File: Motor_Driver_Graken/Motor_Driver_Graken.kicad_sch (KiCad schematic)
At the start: 0 parts

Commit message: Break resistor and IC details
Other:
- added sheet IC Details (IC_Details.kicad_sch)
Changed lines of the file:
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@@
+	)
+	(sheet
+		(at 236.982 80.01)
+		(size 43.434 33.274)
+		(exclude_from_sim no)
+		(in_bom yes)
+		(on_board yes)
+		(dnp no)
+		(fields_autoplaced yes)
+		(stroke
+			(width 0.1524)
+			(type solid)
+		)
+		(fill
+			(color 0 0 0 0.0000)
+		)
+		(property "Sheetname" "IC Details"
+			(at 236.982 79.2984 0)
+			(effects
+				(font
+					(size 1.27 1.27)
+				)
+				(justify left bottom)
+			)
+		)
+		(property "Sheetfile" "IC_Details.kicad_sch"
+			(at 236.982 113.8686 0)
+			(effects
+				(font
+					(size 1.27 1.27)
+				)
+				(justify left top)
+			)
+		)
+		(instances
+			(project "Motor_Driver_Graken"
+				(path "/7c9d4969-3cbd-46ca-8216-6f71fd9792b9"
+					(page "9")
+				)
+			)
+		)
 	)
 	(sheet

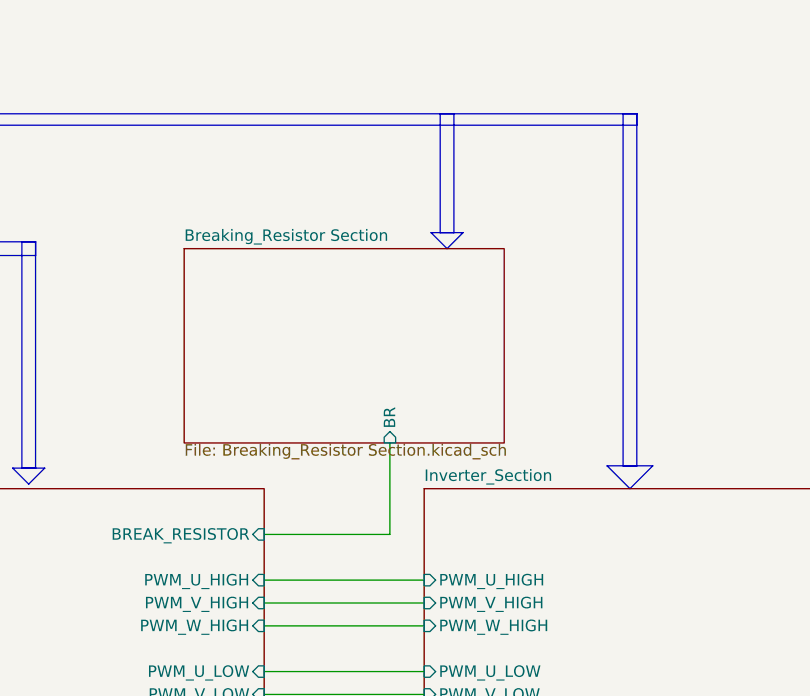
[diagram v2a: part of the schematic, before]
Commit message: Brake resistor Changes
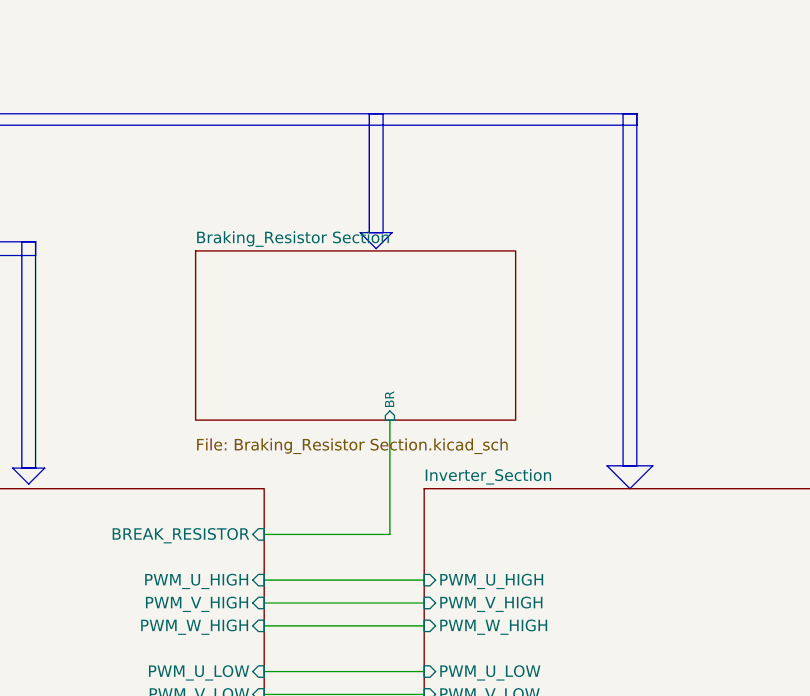
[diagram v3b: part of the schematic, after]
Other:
- sheet Breaking_Resistor Section renamed Braking_Resistor Section
- sheet Braking_Resistor Section: file Breaking_Resistor Section.kicad_sch -> Braking_Resistor Section.kicad_sch
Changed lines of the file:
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@@
 	)
 	(rectangle
-		(start 175.768 38.354)
-		(end 177.292 51.562)
+		(start 167.894 38.354)
+		(end 169.418 51.562)
 		(stroke
 			(width 0)
@@
 	(wire
 		(pts
-			(xy 170.18 74.93) (xy 170.18 85.09)
-		)
-		(stroke
-			(width 0)
-			(type default)
-		)
-	)
-	(wire
-		(pts
 			(xy 156.21 125.73) (xy 173.99 125.73)
 		)
@@
 	(polyline
 		(pts
-			(xy 174.752 51.562) (xy 176.53 53.34)
+			(xy 166.878 51.562) (xy 168.656 53.34)
 		)
 		(stroke
@@
 	(polyline
 		(pts
-			(xy 174.752 51.562) (xy 178.308 51.562)
-		)
-		(stroke
-			(width 0)
-			(type default)
-		)
-	)
-	(polyline
-		(pts
-			(xy 178.308 51.562) (xy 176.53 53.34)
+			(xy 166.878 51.562) (xy 170.434 51.562)
+		)
+		(stroke
+			(width 0)
+			(type default)
+		)
+	)
+	(polyline
+		(pts
+			(xy 170.434 51.562) (xy 168.656 53.34)
 		)
 		(stroke
@@
 		(pts
 			(xy 249.682 70.358) (xy 249.936 70.358)
+		)
+		(stroke
+			(width 0)
+			(type default)
+		)
+	)
+	(wire
+		(pts
+			(xy 170.18 72.39) (xy 170.18 85.09)
 		)
 		(stroke
@@
 	)
 	(sheet
-		(at 147.32 53.34)
-		(size 35.56 21.59)
+		(at 148.59 53.594)
+		(size 35.56 18.796)
 		(exclude_from_sim no)
 		(in_bom yes)
 		(on_board yes)
 		(dnp no)
-		(fields_autoplaced yes)
 		(stroke
 			(width 0.1524)
@@
 			(color 203 220 255 1.0000)
 		)
-		(property "Sheetname" "Breaking_Resistor Section"
-			(at 147.32 52.6284 0)
+		(property "Sheetname" "Braking_Resistor Section"
+			(at 148.59 52.8824 0)
 			(effects
 				(font
@@
 			)
 		)
-		(property "Sheetfile" "Breaking_Resistor Section.kicad_sch"
-			(at 147.32 75.0066 0)
+		(property "Sheetfile" "Braking_Resistor Section.kicad_sch"
+			(at 148.59 74.422 0)
 			(effects
 				(font
@@
 		)
 		(pin "BR" input
-			(at 170.18 74.93 270)
-			(effects
-				(font
-					(size 1.27 1.27)
+			(at 170.18 72.39 270)
+			(effects
+				(font
+					(size 1.016 1.016)
 				)
 				(justify left)
